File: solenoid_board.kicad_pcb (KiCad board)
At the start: 2 copper layers, 100 x 93 mm, 42 parts, among them J2 MCU_LEFT_LEGS, J3 MCU_RIGHT_LEGS

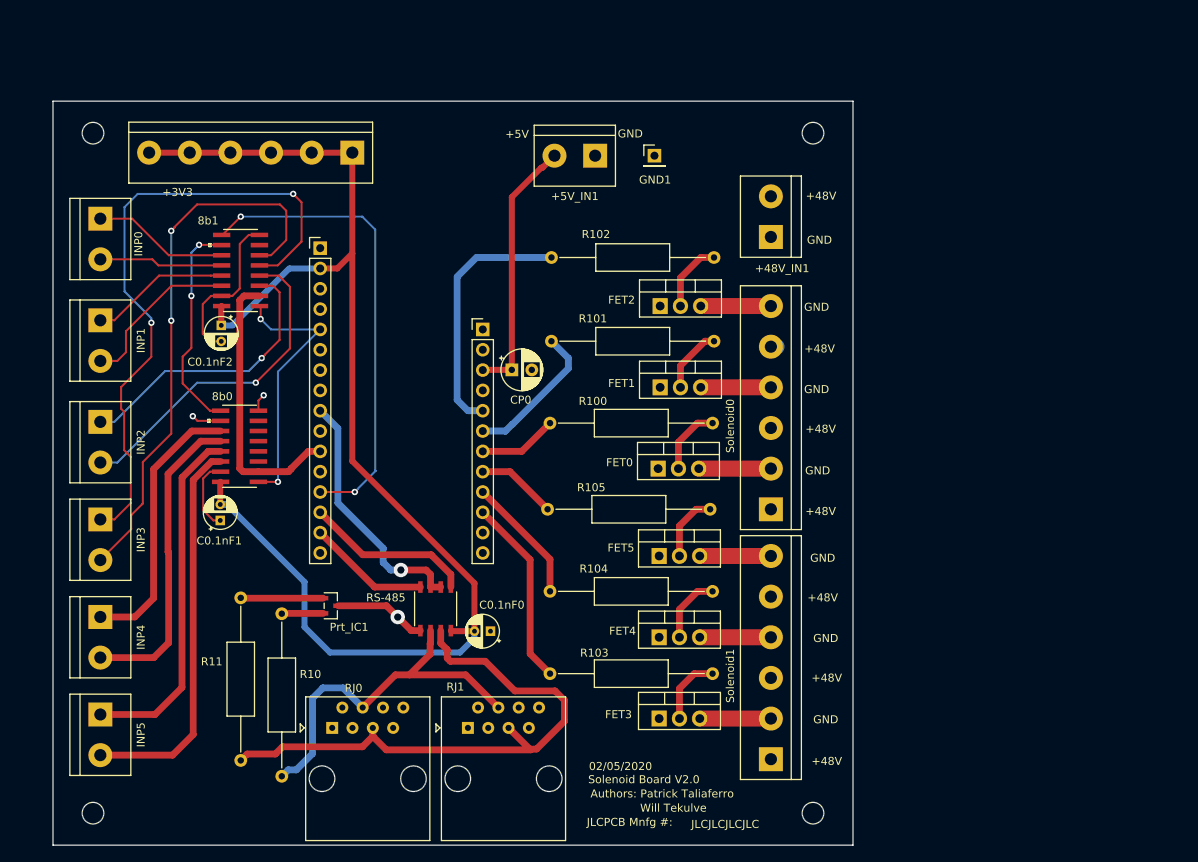
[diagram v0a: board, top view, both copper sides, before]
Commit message: De-Routed all wires to allow for the removal of parts.
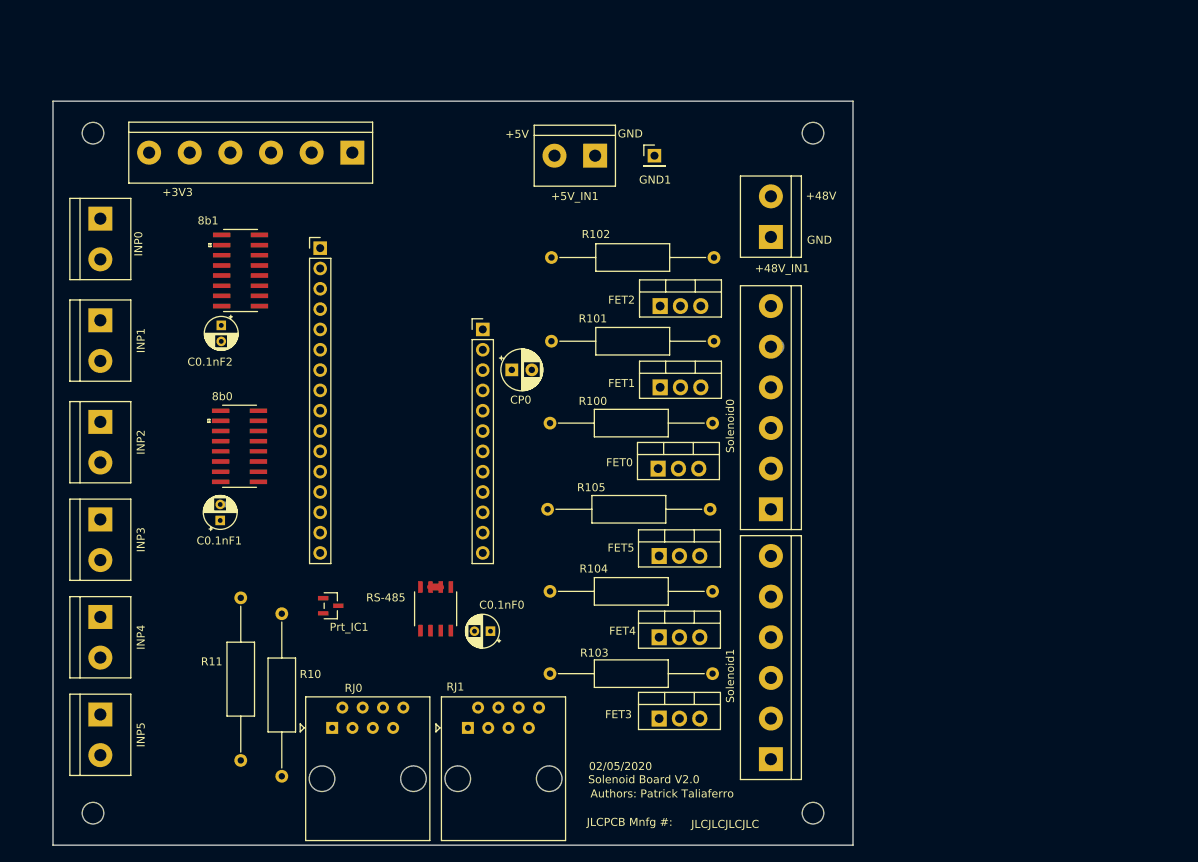
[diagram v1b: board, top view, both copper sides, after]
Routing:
- net +3V3: track 165.4 -> 1.09 mm
- net /INP3_0: track 79.9 -> 0.00 mm, vias 2 -> 0
- net /RJ45_5: track 72.1 -> 0.00 mm
- net /INP3_1: track 68.7 -> 0.00 mm, vias 2 -> 0
- net /MISO: track 59.4 -> 0.00 mm, vias 2 -> 0
- net /INP5_1: track 48.9 -> 0.00 mm
- net GND: track 47.0 -> 0.00 mm, vias 3 -> 0
- net /RJ45_4: track 46.8 -> 0.00 mm
- net /INP5_0: track 44.0 -> 0.00 mm
- net /INP2_1: track 41.7 -> 0.00 mm, vias 1 -> 0
- net /INP4_1: track 38.7 -> 0.00 mm
- net /INP2_0: track 35.5 -> 0.00 mm, vias 1 -> 0
- net /SCK: track 35.0 -> 0.00 mm
- net /INP4_0: track 34.1 -> 0.00 mm
- net /A0: track 33.3 -> 0.00 mm, vias 2 -> 0
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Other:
- board text removed: "Will Tekulve"

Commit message: Swapped out screw terminals for pin headers.
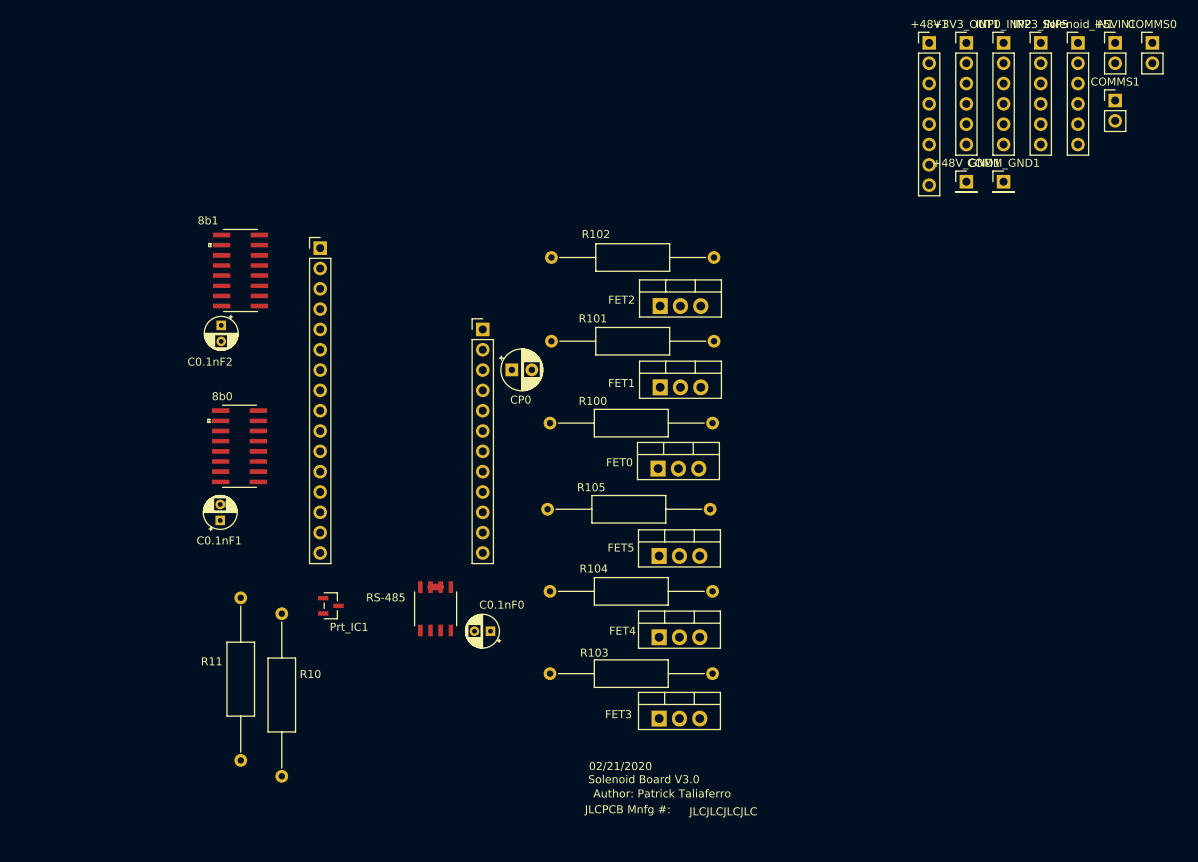
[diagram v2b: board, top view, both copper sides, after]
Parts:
- removed +3V3, Solenoid0, Solenoid1: Screw_Terminal_01x06, TerminalBlock:TerminalBlock_bornier-6_P5.08mm
- removed +48V_IN1: Solenoid_PWR_Supply, TerminalBlock:TerminalBlock_bornier-2_P5.08mm
- removed +5V_IN1: MCU_PWR_Supply, TerminalBlock:TerminalBlock_bornier-2_P5.08mm
- removed GND1: Conn_01x01_Male, Connector_PinHeader_2.54mm:PinHeader_1x01_P2.54mm_Vertical
- removed INP0, INP1, INP2, INP3, INP4, INP5: Screw_Terminal_01x02, TerminalBlock:TerminalBlock_bornier-2_P5.08mm
- removed REF** (x4): MountingHole_2.7mm_M2.5, MountingHole:MountingHole_2.7mm_M2.5
- removed RJ0, RJ1: RJ45, Connector_RJ:RJ45_Amphenol_54602-x08_Horizontal
- added +3V3_OUT1: Conn_01x06, Connector_PinHeader_2.54mm:PinHeader_1x06_P2.54mm_Vertical, F.Cu at (206.2, 45.7)
- added +48V1: Conn_01x08, Connector_PinHeader_2.54mm:PinHeader_1x08_P2.54mm_Vertical, F.Cu at (201.5, 45.7)
- added +48V_GND1: Conn_01x01, Connector_PinHeader_2.54mm:PinHeader_1x01_P2.54mm_Vertical, F.Cu at (206.2, 63.1)
- added +5VIN1: Conn_01x02, Connector_PinHeader_2.54mm:PinHeader_1x02_P2.54mm_Vertical, F.Cu at (224.8, 45.7)
- added COMMS0: Conn_01x02, Connector_PinHeader_2.54mm:PinHeader_1x02_P2.54mm_Vertical, F.Cu at (229.4, 45.7)
- added COMMS1: Conn_01x02, Connector_PinHeader_2.54mm:PinHeader_1x02_P2.54mm_Vertical, F.Cu at (224.8, 52.9)
- added COMM_GND1: Conn_01x01, Connector_PinHeader_2.54mm:PinHeader_1x01_P2.54mm_Vertical, F.Cu at (210.8, 63.1)
- added INP0_INP2: Conn_01x06, Connector_PinHeader_2.54mm:PinHeader_1x06_P2.54mm_Vertical, F.Cu at (210.8, 45.7)
- added INP3_INP5: Conn_01x06, Connector_PinHeader_2.54mm:PinHeader_1x06_P2.54mm_Vertical, F.Cu at (215.5, 45.7)
- added Solenoid_IN1: Conn_01x06, Connector_PinHeader_2.54mm:PinHeader_1x06_P2.54mm_Vertical, F.Cu at (220.1, 45.7)
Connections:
- net /RJ45_4 renamed /A
- net /RJ45_5 renamed /B
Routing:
- net +48V: track 1.07 -> 0.00 mm
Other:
- board outline removed
- board text added: "02/21/2020"
- board text added: "Author: Patrick Taliaferro"
- board text added: "Solenoid Board V3.0"
- board text removed: "+48V"
- board text removed: "+5V"
- board text removed: "02/05/2020"
- board text removed: "Authors: Patrick Taliaferro"
- board text removed: "GND"
- board text removed: "Solenoid Board V2.0"

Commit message: Changed Resistor Footprint to save space. Need to rename symbolic connections to allow for better routing.
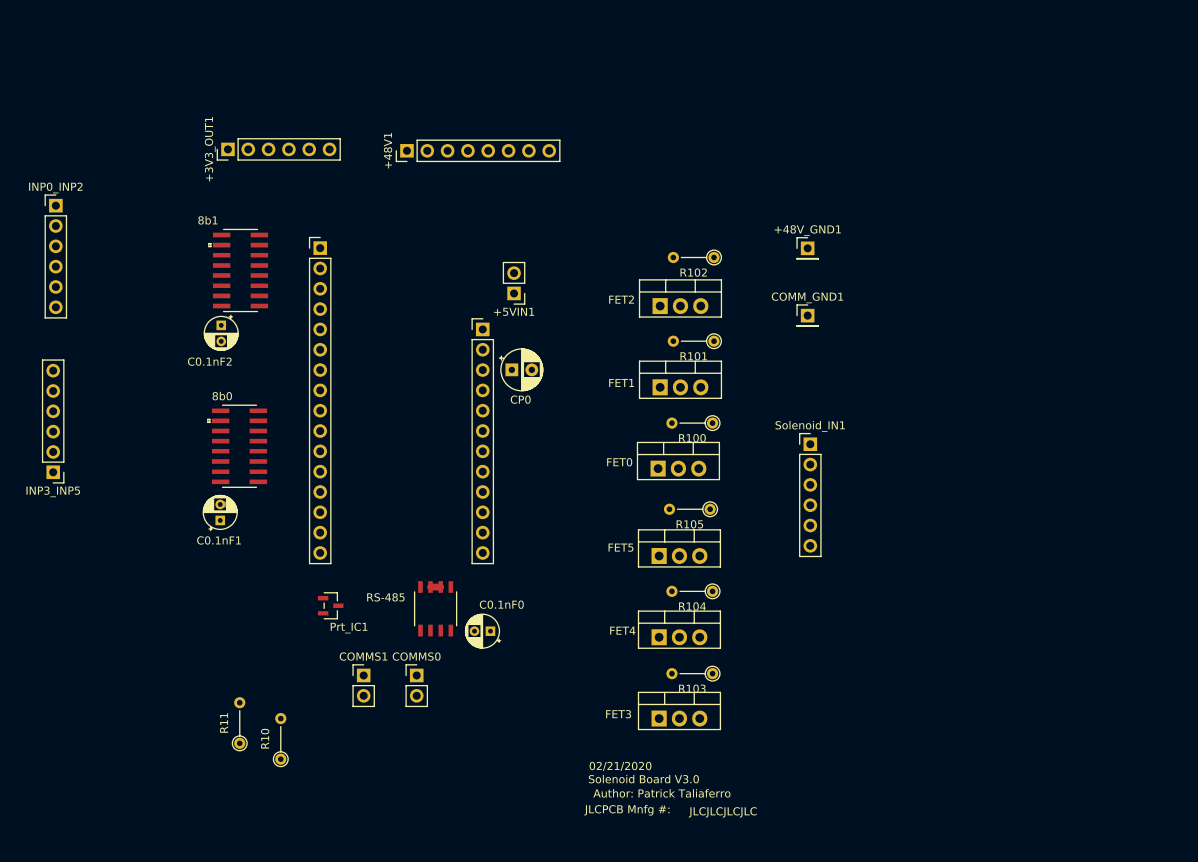
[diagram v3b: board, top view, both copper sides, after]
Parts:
- R10, R100, R101, R102, R103, R104, R105, R11: footprint Resistor_THT:R_Axial_DIN0309_L9.0mm_D3.2mm_P20.32mm_Horizontal -> Resistor_THT:R_Axial_DIN0204_L3.6mm_D1.6mm_P5.08mm_Vertical
- moved INP3_INP5 134.6 mm to (92.0, 99.4), turned to 180 degrees
- moved COMMS0 121.3 mm to (137.5, 124.8)
- moved INP0_INP2 120.2 mm to (92.4, 66.1)
- moved COMMS1 118.3 mm to (130.8, 124.8)
- moved +3V3_OUT1 93.3 mm to (113.9, 59.0), turned to 90 degrees
- moved +5VIN1 81.4 mm to (149.6, 77.0), turned to 180 degrees
- moved +48V1 66.7 mm to (136.2, 59.2), turned to 90 degrees
- moved Solenoid_IN1 60.3 mm to (186.7, 95.9)
- moved COMM_GND1 29.7 mm to (186.3, 79.8)
- moved +48V_GND1 21.5 mm to (186.3, 71.4)
- moved R11 2.14 mm to (115.3, 133.3)
- moved R10 2.14 mm to (120.5, 135.3)

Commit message: Changed pin labels around, re-routed MosFET area, need to route the 8-bit shifter and comms areas.
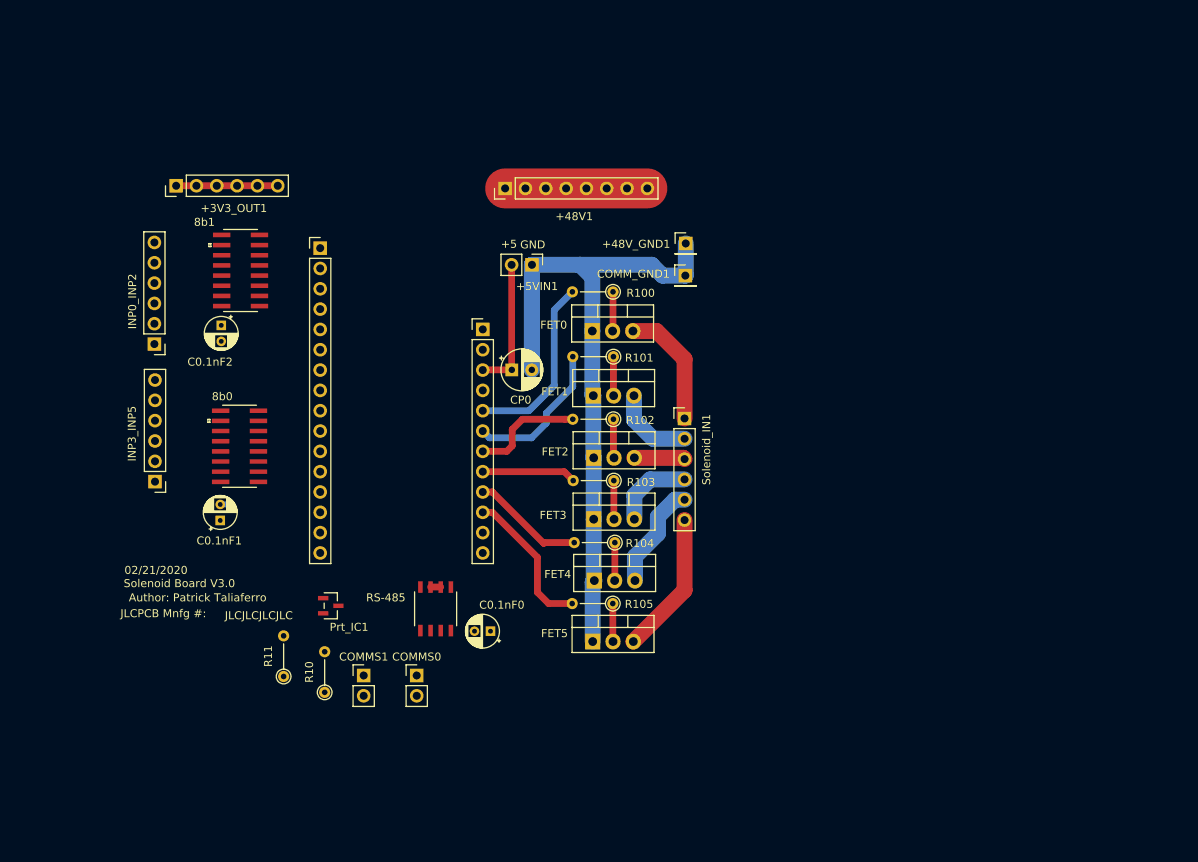
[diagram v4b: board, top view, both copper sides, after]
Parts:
- moved R103 27.1 mm to (162.1, 100.4)
- moved FET3 26.2 mm to (159.6, 105.3)
- moved R102 23.8 mm to (162.1, 92.8)
- moved INP0_INP2 21.2 mm to (104.7, 83.4), turned to 180 degrees
- moved FET2 20.7 mm to (159.6, 97.6)
- moved R100 20.6 mm to (162.0, 76.8)
- moved FET0 19.1 mm to (159.4, 81.7)
- moved R105 16.9 mm to (162.0, 115.8)
- moved COMM_GND1 16.1 mm to (171.0, 74.8)
- moved Solenoid_IN1 16.1 mm to (170.9, 92.7)
- moved +48V_GND1 15.3 mm to (171.1, 70.8)
- moved R104 13.7 mm to (162.2, 108.2)
- moved FET5 13.5 mm to (159.5, 120.5)
- moved +48V1 13.1 mm to (148.5, 63.9)
- moved INP3_INP5 12.8 mm to (104.7, 100.6)
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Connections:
- +48V_GND1 pad 1: (no net) -> GND
- COMM_GND1 pad 1: (no net) -> GND
- INP0_INP2 pad 1: /INP2_0 -> /INP2_1
- INP0_INP2 pad 2: /INP2_1 -> /INP2_0
- INP0_INP2 pad 3: /INP1_0 -> /INP1_1
- INP0_INP2 pad 4: /INP1_1 -> /INP1_0
- INP0_INP2 pad 5: /INP0_0 -> /INP0_1
- INP0_INP2 pad 6: /INP0_1 -> /INP0_0
- INP3_INP5 pad 1: /INP5_0 -> /INP5_1
- INP3_INP5 pad 2: /INP5_1 -> /INP5_0
- INP3_INP5 pad 3: /INP4_0 -> /INP4_1
- INP3_INP5 pad 4: /INP4_1 -> /INP4_0
- INP3_INP5 pad 5: /INP3_0 -> /INP3_1
- INP3_INP5 pad 6: /INP3_1 -> /INP3_0
- R100 pad 2: /D10 -> /D12
- R102 pad 2: /D12 -> /D10
- R103 pad 2: /D5 -> /D9
- R105 pad 2: /D9 -> /D5
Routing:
- net GND: track 0.00 -> 84.8 mm
- net /D12: track 0.00 -> 22.9 mm
- net /D11: track 0.00 -> 18.7 mm
- net /D5: track 0.00 -> 18.5 mm
- net Net-(FET5-Pad3): track 0.00 -> 17.8 mm
- net +48V: track 0.00 -> 17.8 mm
- net +5V: track 0.00 -> 16.8 mm
- net Net-(FET0-Pad3): track 0.00 -> 15.3 mm
- net /D6: track 0.00 -> 14.1 mm
- net /D10: track 0.00 -> 14.1 mm
- net Net-(FET4-Pad3): track 0.00 -> 13.4 mm
- net +3V3: track 1.09 -> 13.8 mm
- net /D9: track 0.00 -> 11.8 mm
- net Net-(FET1-Pad3): track 0.00 -> 10.3 mm
- net Net-(FET3-Pad3): track 0.00 -> 10.1 mm
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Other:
- board text added: "+5"
- board text added: "GND"

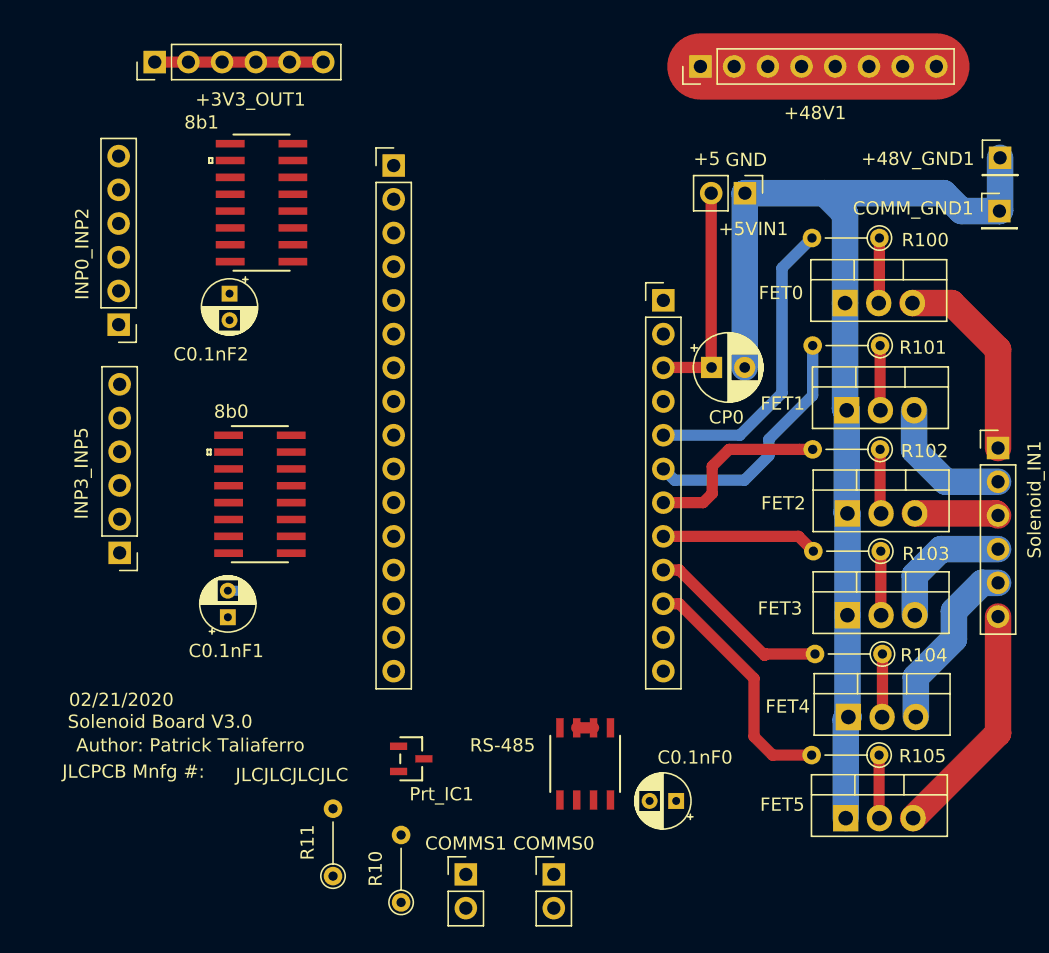
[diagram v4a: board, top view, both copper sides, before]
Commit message: Changed Comms area Geometry. Routed wires for Comms.
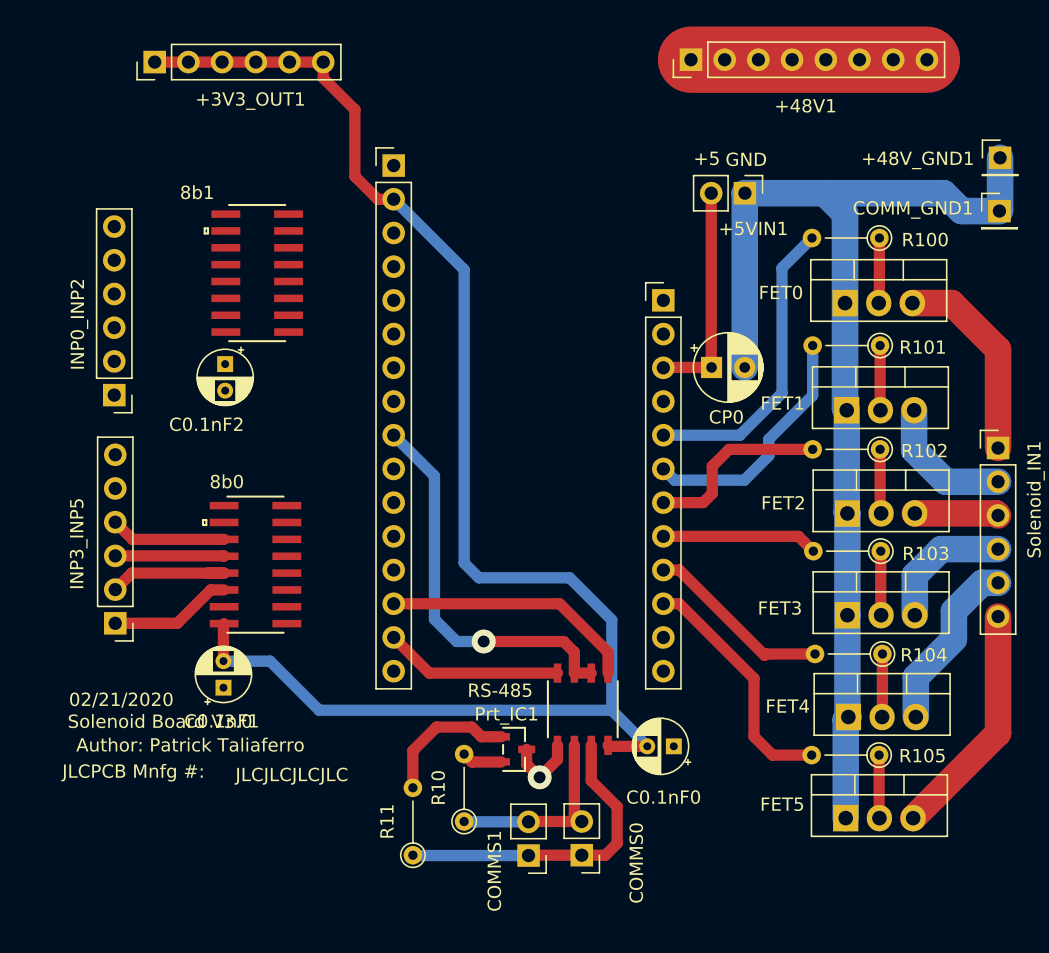
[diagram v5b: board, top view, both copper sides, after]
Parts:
- moved Prt_IC1 7.78 mm to (134.5, 115.4)
- moved R10 7.73 mm to (130.7, 120.8)
- moved R11 6.22 mm to (126.8, 123.3)
- moved INP0_INP2 5.32 mm to (104.3, 88.7)
- moved 8b0 5.32 mm to (115.0, 101.4)
- moved 8b1 5.32 mm to (115.1, 79.5)
- moved C0.1nF1 5.32 mm to (112.6, 110.7)
- moved C0.1nF2 5.32 mm to (112.7, 86.3)
- moved INP3_INP5 5.32 mm to (104.4, 105.9)
- moved COMMS1 4.93 mm to (135.6, 123.4), turned to 180 degrees
- moved C0.1nF0 4.12 mm to (146.5, 115.1)
- moved RS-485 4.12 mm to (139.6, 112.3)
- moved COMMS0 2.56 mm to (139.6, 123.3), turned to 180 degrees
- moved +48V1 0.87 mm to (147.8, 63.4)
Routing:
- net +3V3: track 13.8 -> 116.8 mm
- net /A4: track 1.27 -> 29.6 mm, vias 0 -> 1
- net /B: track 0.00 -> 24.0 mm
- net /RX0: track 0.00 -> 19.2 mm
- net /A: track 0.00 -> 14.9 mm
- net /TX1: track 0.00 -> 13.5 mm
- net Net-(Prt_IC1-Pad1): track 0.00 -> 10.5 mm
- net /INP5_0: track 0.00 -> 9.95 mm
- net /INP5_1: track 0.00 -> 9.25 mm
- net /INP4_0: track 0.00 -> 8.74 mm
- net /INP4_1: track 0.00 -> 8.21 mm
- net GND: track 84.8 -> 90.3 mm, vias 0 -> 1
- net Net-(Prt_IC1-Pad2): track 0.00 -> 3.05 mm
